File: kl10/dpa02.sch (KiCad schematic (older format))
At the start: 15 parts

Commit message: checkpoint
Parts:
- gave numbers to parts that had none: 1
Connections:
- net arxm-sel-1 renamed [n/18+1,ctl-arxl-sel-1,ctl-arxr-sel-1]
- net arxm-sel-2 renamed [n/18+1,ctl-arxl-sel-2,ctl-arxr-sel-2]
- net arxm-sel-4 renamed cram-arxm-sel-4.[n/18+1,0,6]
- net arxm.0-d7 renamed [(n+199)/100,ad.34,adx.[n-2]]
- net arxm.1-d7 renamed [(n+199)/100,ad.35,adx.[n-1]]
- net arxm.5-d5 renamed [n/30+1,adx.[n+6] h,mq.0]
- net mqm.0-d00 renamed [(n+199)/100,adx.34,mq.[n-2]]
- net mqm.0-d10 renamed [(n+199)/100,adx.35,mq.[n-1]]
- net mqm.3-5-dr renamed [n/30+1,mq.[n+6],ad-cry-02]

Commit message: DPA seems to be "done-ish"
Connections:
- net mq.3 is gone; now on net mq.[n+3]: e15.14 (Q1), e35.13 (Y0), e42.3 (X3)
- net mq.[n+3]: now reaches e15.14 (Q1)
- net ad.0 renamed ad.[n+0]
- net ad.1 renamed ad.[n+1]
- net ad.2 renamed ad.[n+2]
- net ad.3 renamed ad.[n+3]
- net ad.4 renamed ad.[n+4]
- net ad.5 renamed ad.[n+5]
- net adx.0 renamed adx.[n+0]
- net adx.1 renamed adx.[n+1]
- net adx.2 renamed adx.[n+2]
- net adx.3 renamed adx.[n+3]
- net adx.4 renamed adx.[n+4]
- net adx.5 renamed adx.[n+5]
- net arx.0 renamed arx.[n+0]
- net arx.1 renamed arx.[n+1]
- net arx.2 renamed arx.[n+2]
- net arx.3 renamed arx.[n+3]
- net arx.4 renamed arx.[n+4]
- net arx.5 renamed arx.[n+5]
- net arxm.0 renamed arxm.[n+0]
- net arxm.1 renamed arxm.[n+1]
- net arxm.2 renamed arxm.[n+2]
- net arxm.3 renamed arxm.[n+3]
- net arxm.4 renamed arxm.[n+4]
- net arxm.5 renamed arxm.[n+5]
- net cache-data.0 renamed cache-data.[n+0]
- net cache-data.1 renamed cache-data.[n+1]
- net cache-data.2 renamed cache-data.[n+2]
- net cache-data.3 renamed cache-data.[n+3]
- net cache-data.4 renamed cache-data.[n+4]
- net cache-data.5 renamed cache-data.[n+5]
- net mq.0 renamed mq.[n+0]
- net mq.1 renamed mq.[n+1]
- net mq.2 renamed mq.[n+2]
- net mq.4 renamed mq.[n+4]
- net mq.5 renamed mq.[n+5]
- net mqm.0 renamed mqm.[n+0]
- net mqm.1 renamed mqm.[n+1]
- net mqm.2 renamed mqm.[n+2]
- net mqm.3 renamed mqm.[n+3]
- net mqm.4 renamed mqm.[n+4]
- net mqm.5 renamed mqm.[n+5]
- net sh.0 renamed sh.[n+0]
- net sh.1 renamed sh.[n+1]
- net sh.2 renamed sh.[n+2]
- net sh.3 renamed sh.[n+3]
- net sh.4 renamed sh.[n+4]
- net sh.5 renamed sh.[n+5]

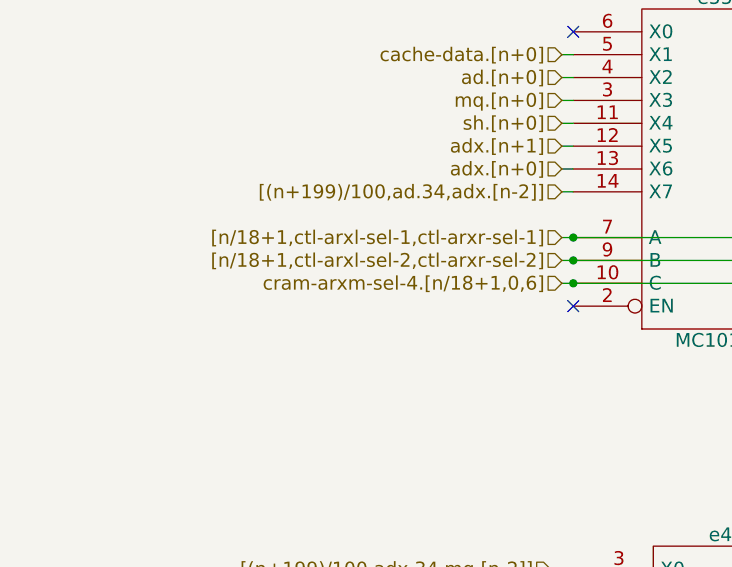
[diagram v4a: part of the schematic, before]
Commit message: Fix leading zeros in name
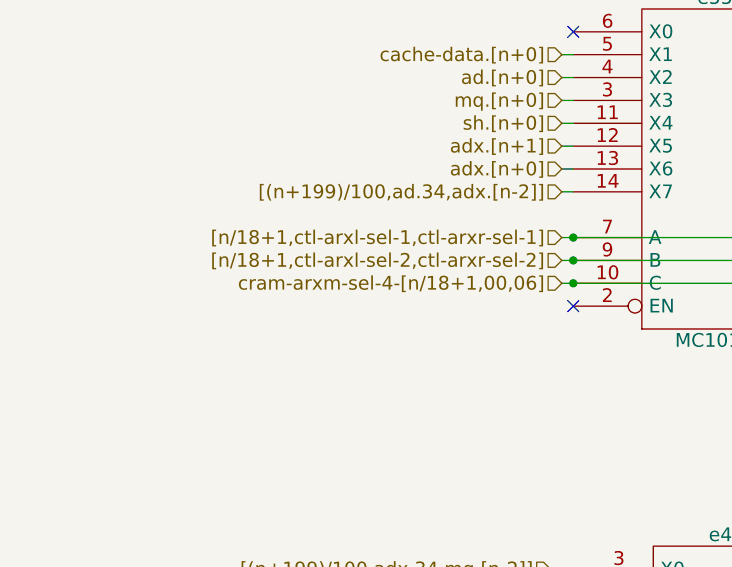
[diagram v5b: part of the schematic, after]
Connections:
- net cram-arxm-sel-4.[n/18+1,0,6] renamed cram-arxm-sel-4-[n/18+1,00,06]
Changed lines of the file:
@@
 [n/18+1,ctl-arxl-sel-2,ctl-arxr-sel-2]
 Text HLabel 3000 4550 0    60   Input ~ 0
-cram-arxm-sel-4.[n/18+1,0,6]
+cram-arxm-sel-4-[n/18+1,00,06]
 Wire Wire Line
 	3000 4450 5400 4450

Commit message: Update to kicad 5.1.2
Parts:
- e13, e15, e25, e32: symbol MC10141 -> o_ecl:MC10141
- e24, e38: symbol MC10101 -> o_ecl:MC10101
- e30, e31, e42, e49, e55, e56: symbol MC10164 -> o_ecl:MC10164
- e35, e45, e48: symbol MC10174 -> o_ecl:MC10174
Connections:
- net [n/18+1,ctl-arxl-sel-1,ctl-arxr-sel-1]: no longer e31.7 (A), e42.7 (A), e49.7 (A), e56.7 (A)
- net [n/18+1,ctl-arxl-sel-2,ctl-arxr-sel-2]: no longer e31.9 (B), e42.9 (B), e49.9 (B), e56.9 (B)
- net cram-arxm-sel-4-[n/18+1,00,06]: no longer e31.10 (C), e42.10 (C), e49.10 (C), e56.10 (C)
- net ctl-mqm-sel-1: no longer e48.7 (A)
- net ctl-mqm-sel-2: no longer e48.9 (B)
- net at e35.10 (Y3), e35.6 (X3), e38.9 (O)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: no longer e48.10 (Y3), e48.6 (X3)
- net at e35.14 (EN), e38.15 (O), e45.14 (EN): no longer e48.14 (EN)
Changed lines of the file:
@@
-EESchema Schematic File Version 2
-LIBS:o_ecl
-LIBS:ecl
-LIBS:power
-LIBS:device
-LIBS:transistors
-LIBS:conn
-LIBS:linear
-LIBS:regul
-LIBS:74xx
-LIBS:cmos4000
-LIBS:adc-dac
-LIBS:memory
-LIBS:xilinx
-LIBS:microcontrollers
-LIBS:dsp
-LIBS:microchip
-LIBS:analog_switches
-LIBS:motorola
-LIBS:texas
-LIBS:intel
-LIBS:audio
-LIBS:interface
-LIBS:digital-audio
-LIBS:philips
-LIBS:display
-LIBS:cypress
-LIBS:siliconi
-LIBS:opto
-LIBS:atmel
-LIBS:contrib
-LIBS:valves
+EESchema Schematic File Version 4
 LIBS:kl10-cache
-EELAYER 25 0
+EELAYER 30 0
 EELAYER END
 $Descr B 17000 11000
@@
 $EndDescr
 $Comp
-L MC10141 e25
+L o_ecl:MC10141 e25
 U 1 1 57ACA2E8
 P 5450 1500
@@
 NoConn ~ 4850 1550
 Wire Wire Line
-	4850 1850 4850 2200
+	4850 1850 4850 1950
 Text HLabel 4800 1750 2    60   Input ~ 0
 dp04-clk
@@
 	4800 1750 4850 1750
 $Comp
-L MC10101 e24
+L o_ecl:MC10101 e24
 U 3 1 57ACA62E
 P 4100 2300
@@
 $EndComp
 Wire Wire Line
-	8050 2200 4700 2200
+	8050 2200 4850 2200
 Connection ~ 4850 1950
 Text HLabel 3450 2200 2    60   Input ~ 0
@@
 	6050 1450 6100 1450
 $Comp
-L MC10141 e32
+L o_ecl:MC10141 e32
 U 1 1 57ACAB89
 P 8650 1500
@@
 NoConn ~ 8050 1550
 Wire Wire Line
-	8050 1850 8050 2200
+	8050 1850 8050 1950
 Text HLabel 8000 1750 2    60   Input ~ 0
 dp04-clk
@@
 	8050 1150 7950 1150
 $Comp
-L MC10164 e55
+L o_ecl:MC10164 e55
 U 1 1 57ACAFFC
 P 3650 4050
@@
 cram-arxm-sel-4-[n/18+1,00,06]
 Wire Wire Line
-	3000 4450 5400 4450
-Wire Wire Line
-	3000 4550 5400 4550
+	3000 4450 3050 4450
+Wire Wire Line
+	3000 4550 3050 4550
 NoConn ~ 3050 4650
 $Comp
-L MC10164 e56
+L o_ecl:MC10164 e56
 U 1 1 57ACB70A
 P 6000 4050
@@
 Connection ~ 3050 4550
 Wire Wire Line
-	3000 4350 7700 4350
-Wire Wire Line
-	4900 4450 7700 4450
-Wire Wire Line
-	4900 4550 7700 4550
-$Comp
-L MC10164 e49
+	3000 4350 3050 4350
+$Comp
+L o_ecl:MC10164 e49
 U 1 1 57ACBC44
 P 8300 4050
@@
 Wire Wire Line
 	7650 4150 7700 4150
-Wire Wire Line
-	7050 4350 9850 4350
-Wire Wire Line
-	7050 4450 9850 4450
-Wire Wire Line
-	7050 4550 9850 4550
-$Comp
-L MC10164 e42
+$Comp
+L o_ecl:MC10164 e42
 U 1 1 57ACC128
 P 10450 4050
@@
 Wire Wire Line
 	9800 4150 9850 4150
-Wire Wire Line
-	4900 4350 5400 4350
 Connection ~ 4900 4350
-Connection ~ 4900 4450
-Connection ~ 4900 4550
-Connection ~ 7050 4350
 Connection ~ 7050 4450
 Connection ~ 7050 4550
-Wire Wire Line
-	9300 4350 12100 4350
-Wire Wire Line
-	9300 4450 12100 4450
-Wire Wire Line
-	9300 4550 12100 4550
-$Comp
-L MC10164 e31
+$Comp
+L o_ecl:MC10164 e31
 U 1 1 57ACCDCD
 P 12700 4050
@@
 	12050 4150 12100 4150
 Connection ~ 9300 4350
-Connection ~ 9300 4450
-Connection ~ 9300 4550
-Wire Wire Line
-	11550 4350 14350 4350
-Wire Wire Line
-	11550 4450 14350 4450
-Wire Wire Line
-	11550 4550 14350 4550
-$Comp
-L MC10164 e30
+$Comp
+L o_ecl:MC10164 e30
 U 1 1 57ACD533
 P 14950 4050
@@
 Wire Wire Line
 	14300 4150 14350 4150
-Connection ~ 11550 4350
 Connection ~ 11550 4450
 Connection ~ 11550 4550
@@
 [n/30+1,adx.[n+6] h,mq.0]
 $Comp
-L MC10174 e45
+L o_ecl:MC10174 e45
 U 1 1 57ACDEF5
 P 3700 6300
@@
 $EndComp
 $Comp
-L MC10101 e38
+L o_ecl:MC10101 e38
 U 4 1 57ACDF63
 P 2200 7150
@@
 	2800 7050 2800 6800
 Wire Wire Line
-	2800 6800 5650 6800
+	2800 6800 3100 6800
 Wire Wire Line
 	3050 7250 2800 7250
 Wire Wire Line
-	3050 6100 3050 7250
-Wire Wire Line
-	3050 6100 5650 6100
+	3050 6100 3050 6500
+Wire Wire Line
+	3050 6100 3100 6100
 Text HLabel 1550 7050 0    60   Input ~ 0
 ctl-mqm-en
@@
 ctl-mqm-sel-1
 Wire Wire Line
-	2950 6700 5650 6700
-Wire Wire Line
-	2950 6600 5650 6600
+	2950 6700 3100 6700
+Wire Wire Line
+	2950 6600 3100 6600
 Text HLabel 2950 6200 0    60   Input ~ 0
 [(n+199)/100,adx.35,mq.[n-1]]
@@
 	2950 6400 3100 6400
 Wire Wire Line
-	3050 6500 5650 6500
+	3050 6500 3100 6500
 Connection ~ 3050 6500
 Text HLabel 4350 5800 2    60   Input ~ 0
@@
 	4300 6200 4350 6200
 $Comp
-L MC10174 e48
+L o_ecl:MC10174 e48
 U 1 1 57ACF507
 P 6250 6300
@@
 Wire Wire Line
 	5500 6200 5650 6200
-Wire Wire Line
-	4950 6800 7800 6800
-Wire Wire Line
-	5200 6100 7800 6100
-Wire Wire Line
-	5100 6700 7800 6700
-Wire Wire Line
-	5100 6600 7800 6600
-Wire Wire Line
-	5200 6500 7800 6500
-$Comp
-L MC10174 e35
+$Comp
+L o_ecl:MC10174 e35
 U 1 1 57AD0630
 P 8400 6300
@@
 	7650 6200 7800 6200
 $Comp
-L MC10141 e13
+L o_ecl:MC10141 e13
 U 1 1 57AD0A4E
 P 10750 6250
@@
 	10050 6300 10150 6300
 Wire Wire Line
-	10100 6500 12300 6500
+	10100 6500 10150 6500
 Text HLabel 10100 6600 0    60   Input ~ 0
 ctl-mq-sel-1
@@
 ctl-mq-sel-2
 Wire Wire Line
-	10100 6600 12300 6600
-Wire Wire Line
-	10100 6700 12300 6700
-$Comp
-L MC10141 e15
+	10100 6600 10150 6600
+Wire Wire Line
+	10100 6700 10150 6700
+$Comp
+L o_ecl:MC10141 e15
 U 1 1 57AD1768
 P 12900 6250
@@
 Wire Wire Line
 	12200 6300 12300 6300
+Wire Wire Line
+	4850 1950 4850 2200
+Wire Wire Line
+	8050 1950 8050 2200
+Wire Wire Line
+	4850 2200 4700 2200
+Wire Wire Line
+	3050 6500 3050 7250
+Wire Wire Line
+	10150 6500 12300 6500
+Wire Wire Line
+	10150 6600 12300 6600
+Wire Wire Line
+	10150 6700 12300 6700
+Wire Wire Line
+	3100 6800 7800 6800
+Wire Wire Line
+	3100 6100 7800 6100
+Wire Wire Line
+	3100 6700 7800 6700
+Wire Wire Line
+	3100 6600 7800 6600
+Wire Wire Line
+	3100 6500 7800 6500
+Wire Wire Line
+	3050 4450 14350 4450
+Wire Wire Line
+	3050 4550 14350 4550
+Wire Wire Line
+	3050 4350 14350 4350
 $EndSCHEMATC
